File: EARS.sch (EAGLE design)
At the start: 4 parts, among them IC1 STM32L151RDT

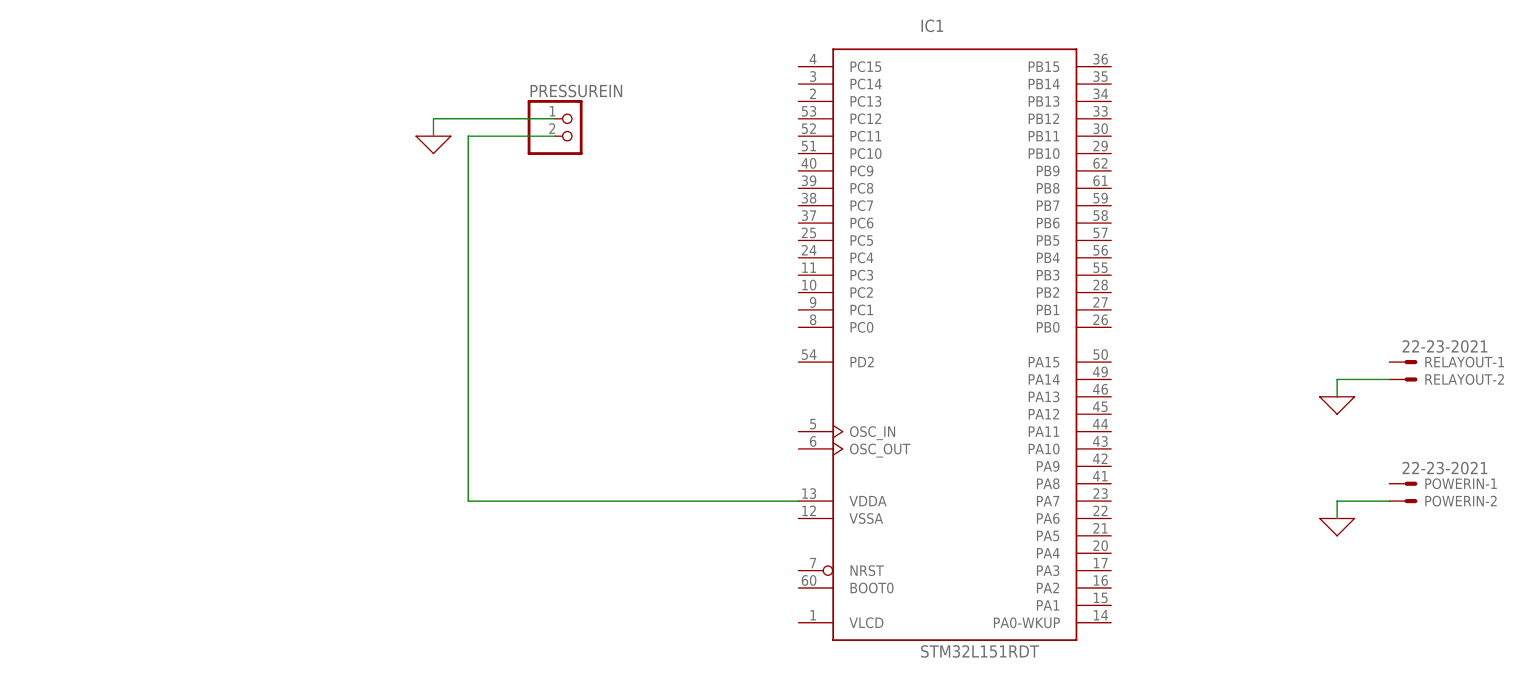
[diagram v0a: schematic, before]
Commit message: Add files via upload
Added step down regulator to Schematic.
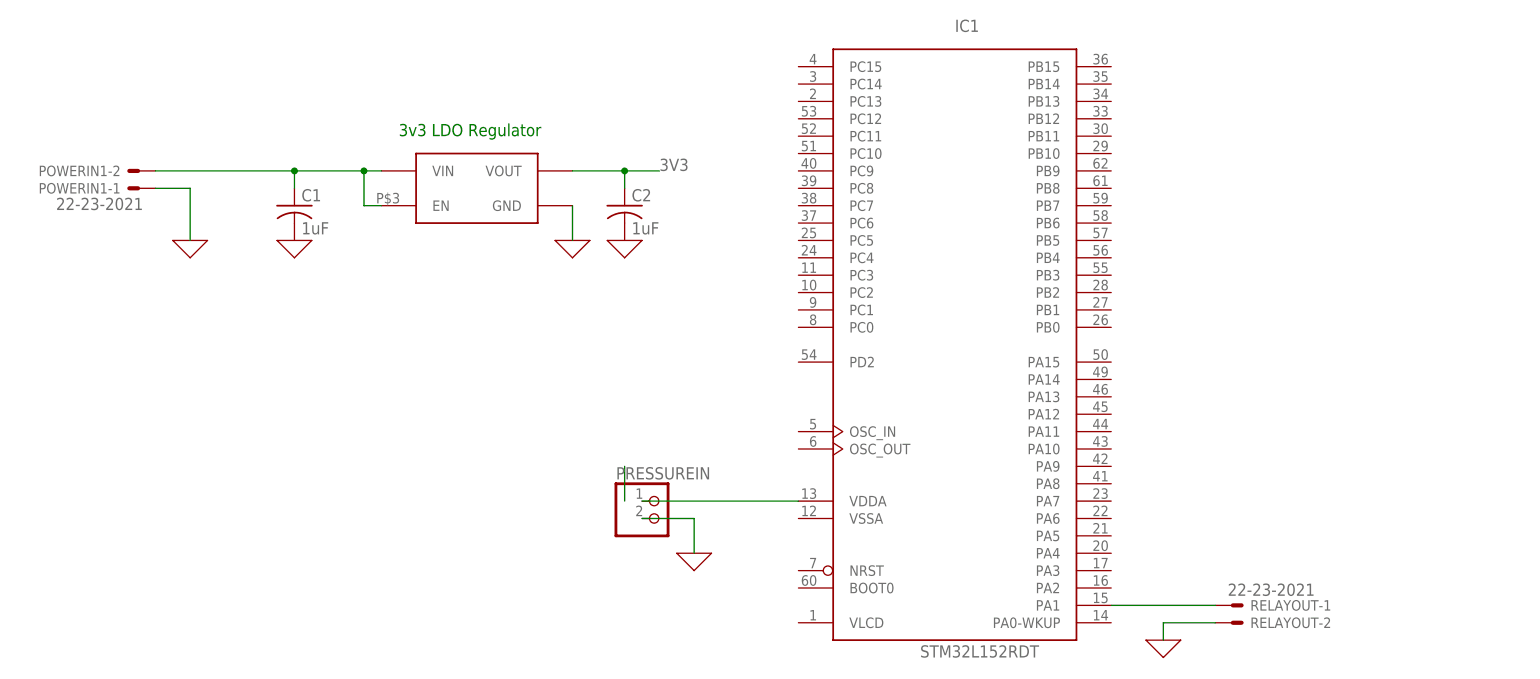
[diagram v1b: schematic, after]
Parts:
- removed POWERIN: 22-23-2021, con-molex:22-23-2021
- added 3V3REG: NCP551, EARS:NCP551
- added C1, C2: 1uF, rcl:C-USC0603
- added POWERIN1: 22-23-2021, con-molex:22-23-2021
- IC1: value STM32L151RDT -> STM32L152RDT; device micro-stm_v3:STM32L151RDT -> micro-stm_v3:STM32L152RDT
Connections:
- new net 3V3: 3V3REG.VOUT, C2.1
- new net N$4: 3V3REG.EN, 3V3REG.VIN, C1.1, POWERIN1-2.S
- new net N$5: IC1MCU.VDDA, PRESSUREIN.1
- net 0: now also 3V3REG.GND, C1.2, C2.2, POWERIN1-1.S, PRESSUREIN.2; no longer POWERIN-2.S, PRESSUREIN.1
- net N$3: now also IC1MCU.PA1, RELAYOUT-1.S; no longer IC1MCU.VDDA, PRESSUREIN.2
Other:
- note added: "3v3 LDO Regulator"
- moved on the sheet: PRESSUREIN, RELAYOUT-1, RELAYOUT-2

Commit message: Initial Layout, fixed schematic.
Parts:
- removed 3V3REG: NCP551, EARS:NCP551
- removed IC1: STM32L152RDT, micro-stm_v3:STM32L152RDT
- removed POWERIN1, RELAYOUT: 22-23-2021, con-molex:22-23-2021
- removed PRESSUREIN: (no value), pinhead:PINHD-1X2
- added C10: 22u, rcl:C-EUC0603
- added C11: 100n, rcl:C-EUC0603
- added C12, C5, C6, C7: 10u, rcl:C-EUC0603
- added C13: 1u, rcl:C-EUC0603
- added C3, C4: 18p, rcl:C-EUC0603
- added D1: (no value), adafruit:DIODESMA
- added J1: 1X2-3.5MM, adafruit:1X2-3.5MM
- added J2: CORTEX_DEBUG_SMD, SparkFun-Connectors:CORTEX_DEBUG_SMD
- added JP1: (no value), pinhead:PINHD-1X4
- added JP2: (no value), pinhead:PINHD-1X8
- added L1: 6.8, rcl:L-USL3216C
- added R1: 390, rcl:R-US_R0603
- added R2: 0, rcl:R-US_R0603
- added U$1: STM32LXX, EARS:STM32LXX
- added U$2: LMR160067Q3, EARS:LMR160067Q3
- added X1: ECX_34G, EARS:ECX_34G
- added X2: (no value), EARS:FL0800011Q
- C1, C2: value 1uF -> 6p; device rcl:C-USC0603 -> rcl:C-EUC0603
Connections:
- removed net 0: 3V3REG.GND, C1.2, C2.2, POWERIN1-1.S, PRESSUREIN.2, RELAYOUT-2.S
- removed net N$3: IC1MCU.PA1, RELAYOUT-1.S
- removed net N$4: 3V3REG.EN, 3V3REG.VIN, C1.1, POWERIN1-2.S
- removed net N$5: IC1MCU.VDDA, PRESSUREIN.1
- new net !RESET!: J2.!RESET, U$1.PB4
- new net 12V: C10.2, J1.2, JP1.1, U$2.!SHDN!, U$2.VIN
- new net 8M0X_OUT: C4.2, R1.1, X2.C2
- new net 8MOX_IN: C3.2, U$1.PH0-OSC_IN, X2.C1
- new net GND: C1.1, C10.1, C12.2, C13.1, C2.1, C3.1, C4.1, C5.1, C6.1, C7.1, D1.A, J1.1, J2.GND@3, J2.GND@5, J2.GNDDTCT, JP1.4, U$1.BOOT0, U$1.VSSA, U$1.VSS_1, U$1.VSS_2, U$1.VSS_3, U$2.GND, X1.P$1, X2.P$1
- new net LMR_CB: C11.1, U$2.CB
- new net LMR_SW: C11.2, D1.C, L1.1, U$2.SW
- new net MCU_P4: R2.2, U$1.PC15-OSC32_OUT
- new net MCU_P6: R1.2, U$1.PH1-OSC_OUT
- new net NC: J2.NC/TDI, U$1.PA15
- new net OSC32_IN: C1.2, R2.1, X1.C2
- new net OSC32_OUT: C2.2, U$1.PC14-OSC32_IN, X1.C1
- new net P_IN1: JP2.5, U$1.PA5
- new net P_IN2: JP2.6, U$1.PA6
- new net P_IN3: JP2.7, U$1.PA7
- new net P_IN4: JP2.8, U$1.PB0
- new net P_OUT1: JP2.1, U$1.PA1
- new net P_OUT2: JP2.2, U$1.PA2
- new net P_OUT3: JP2.3, U$1.PA3
- new net P_OUT4: JP2.4, U$1.PA4
- new net SOL_1: JP1.2, U$1.PB13
- new net SOL_2: JP1.3, U$1.PB14
- new net SWDCLK: J2.SWDCLK/TCK, U$1.PA14
- new net SWDIO: J2.SWDIO/TMS, U$1.PA13
- new net SWO: J2.SWO/TDO, U$1.PB3
- net 3V3: now also C12.1, C13.2, C5.2, C6.2, C7.2, J2.VCC, L1.2, U$1.VDDA, U$1.VDD_1, U$1.VDD_2, U$1.VDD_3, U$1.VLCD, U$2.FB; no longer 3V3REG.VOUT, C2.1
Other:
- note added: "12v-3.3v DC-DC Regulator Diode Breakdown 15V"
- note added: "MCU Power Suppy 1uF caps across VDDA-VDDS 10uF Caps across VDD* (1-3)"
- note removed: "3v3 LDO Regulator"
- moved on the sheet: C1, C2
